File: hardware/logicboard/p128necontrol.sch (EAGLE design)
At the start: 57 parts, among them IC1 74LS158N, IC10 74LS595D, IC11 74LS595D, IC12 74LS595D, IC13 74LS595D, IC14 74LS595D, IC15 74LS595D, IC16 74LS595D, IC17 74LS595D, IC2 74LS595D, IC3 74LS595D, IC4 74LS595D, IC5 74LS595D, IC6 74LS595D, IC7 74LS595D, IC8 74LS595D, IC9 74LS595D, J2 DIN5

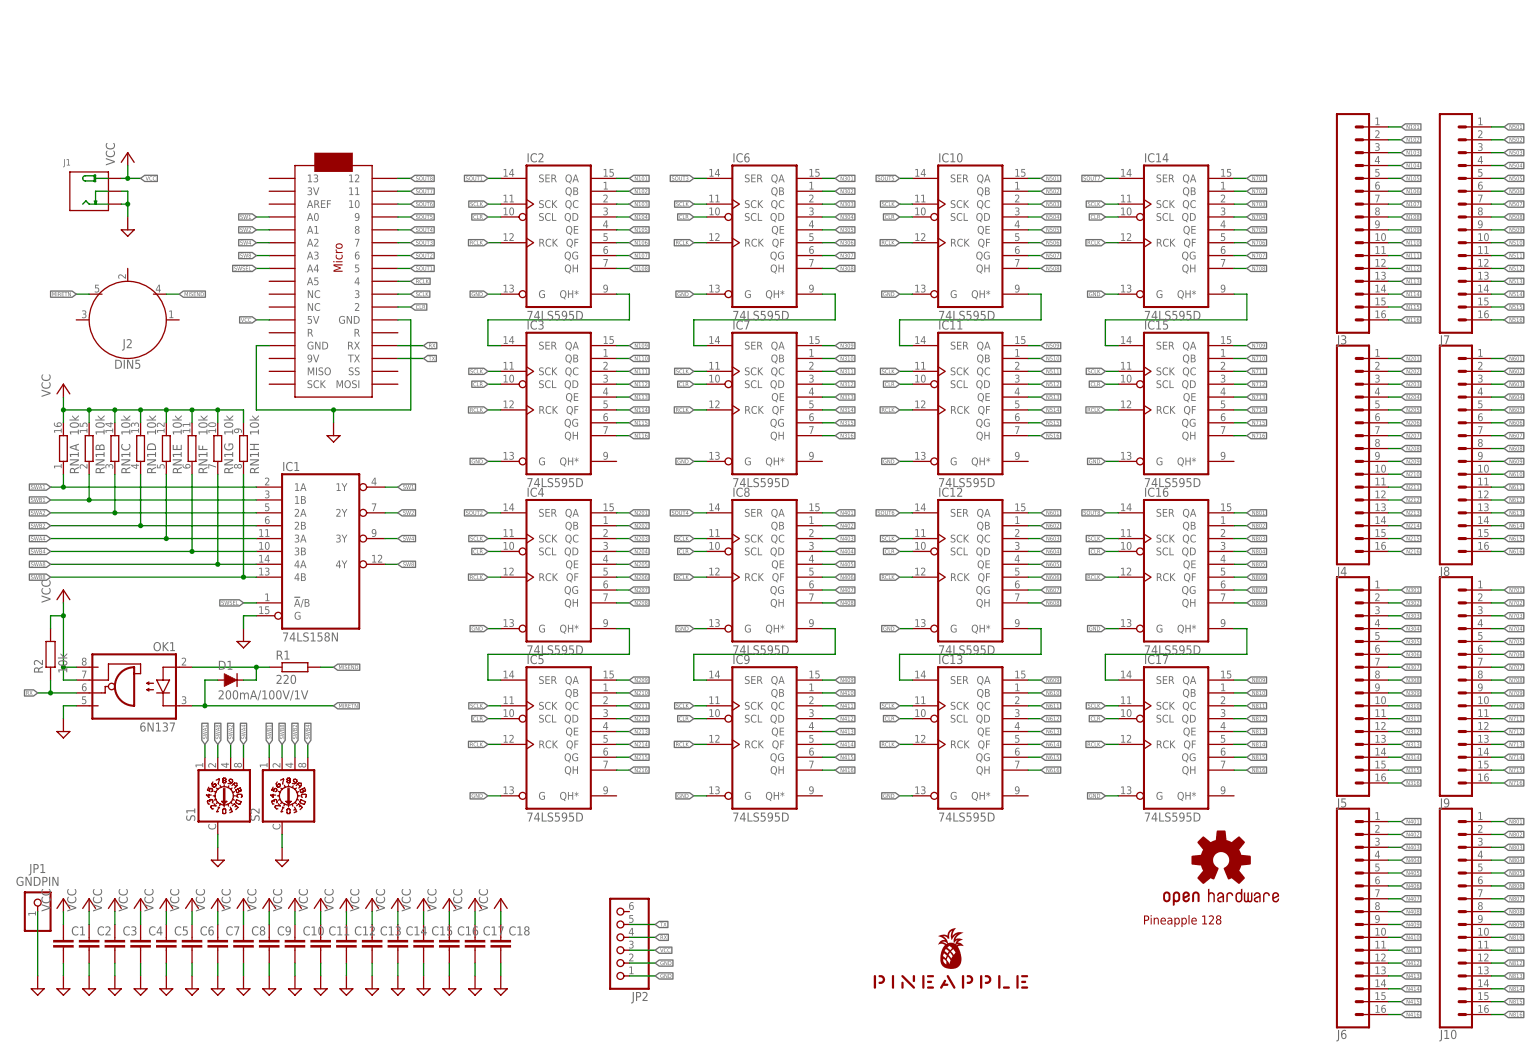
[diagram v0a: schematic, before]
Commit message: Nocontrol 128-ch out.
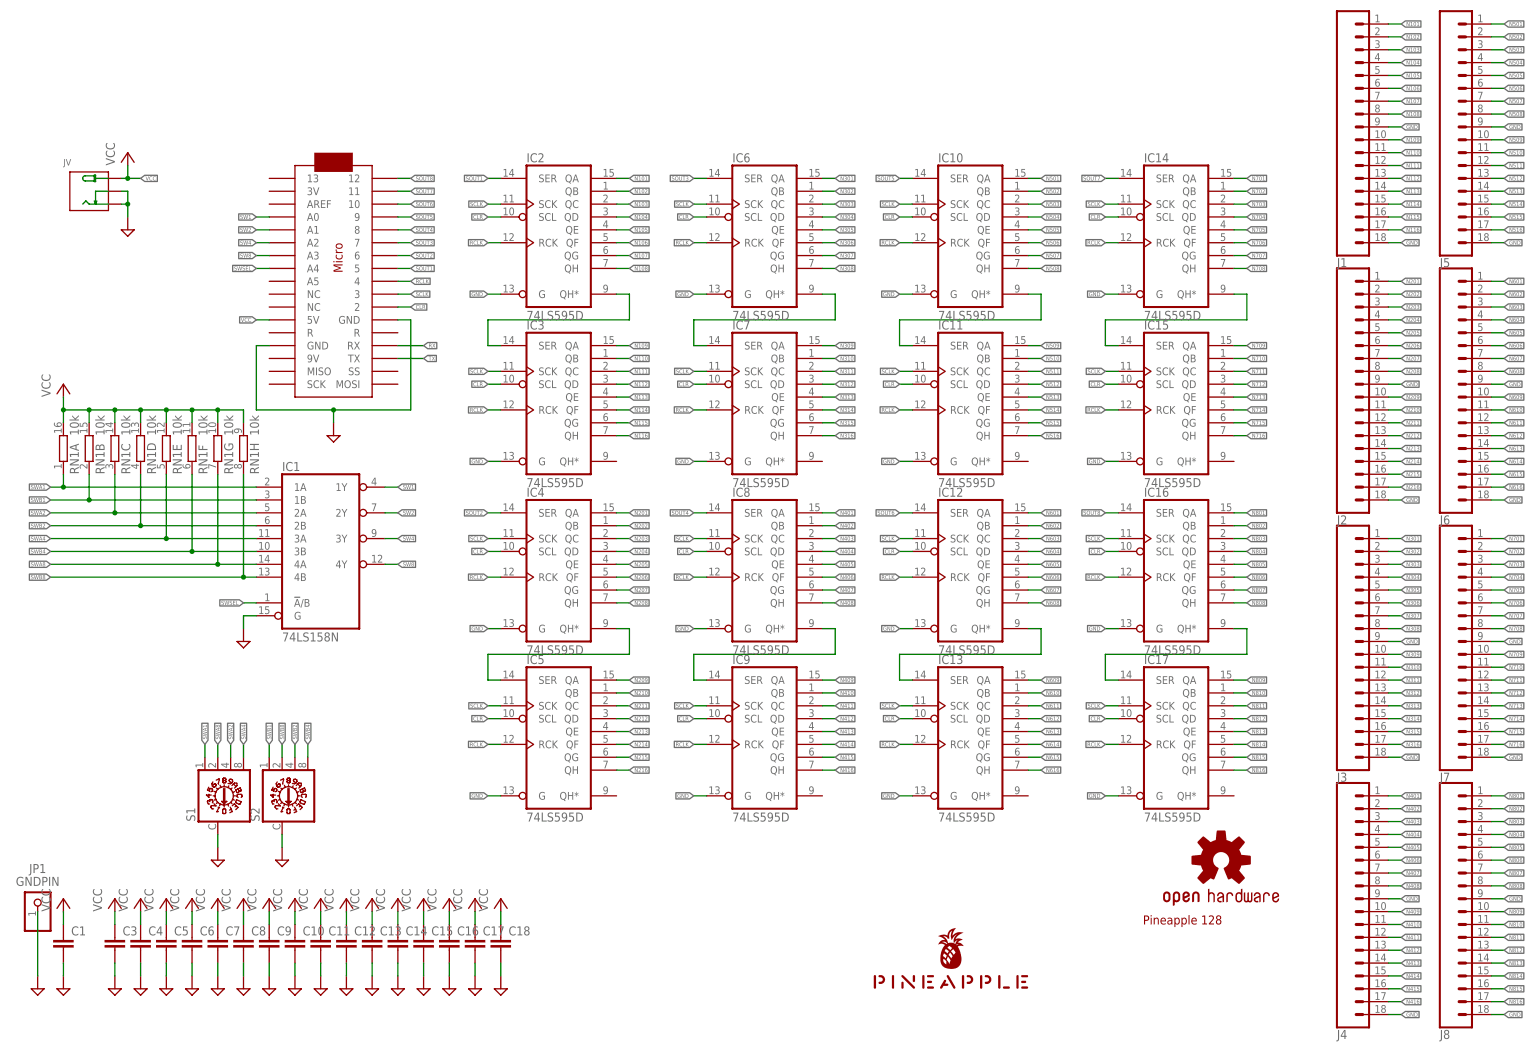
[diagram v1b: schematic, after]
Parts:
- removed C2: (no value), resistor:C-EU025-024X044
- removed D1: 200mA/100V/1V, SparkFun-DiscreteSemi:DIODE-1N4148
- removed J10, J9: (no value), SparkFun-Connectors:CONN_16
- removed JP2: (no value), pinhead:PINHD-1X6
- removed OK1: 6N137, optocoupler:6N137
- removed R1: 220, resistor:R-EU_0204/5
- removed R2: 10k, resistor:R-EU_0204/5
- added JV: (no value), Seeed-Connector:JACK-DC-005'DC-005'
- J1: device Seeed-Connector:JACK-DC-005'DC-005' -> SparkFun-Connectors:CONN_18
- J2: value DIN5 -> (none); device SparkFun-Connectors:DIN5 -> SparkFun-Connectors:CONN_18
- J3, J4, J5, J6, J7, J8: device SparkFun-Connectors:CONN_16 -> SparkFun-Connectors:CONN_18
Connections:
- removed net MIRETN: D1.A, J2.5, OK1.C
- removed net MISEND: J2.4, R1.2
- removed net N$1: D1.C, OK1.A, R1.1
- net GND: now also J1.18, J1.9, J2.18, J2.9, J3.18, J3.9, J4.18, J4.9, J5.18, J5.9, J6.18, J6.9, J7.18, J7.9, J8.18, J8.9, JV.-, JV.CDN; no longer C2.2, J1.-, J1.CDN, JP2.1, JP2.2, OK1.GND
- net N101: now also J1.1; no longer J3.1
- net N102: now also J1.2; no longer J3.2
- net N103: now also J1.3; no longer J3.3
- net N104: now also J1.4; no longer J3.4
- net N105: now also J1.5; no longer J3.5
- net N106: now also J1.6; no longer J3.6
- net N107: now also J1.7; no longer J3.7
- net N108: now also J1.8; no longer J3.8
- net N109: now also J1.10; no longer J3.9
- net N110: now also J1.11; no longer J3.10
- net N111: now also J1.12; no longer J3.11
- net N112: now also J1.13; no longer J3.12
- net N113: now also J1.14; no longer J3.13
- net N114: now also J1.15; no longer J3.14
- net N115: now also J1.16; no longer J3.15
- net N116: now also J1.17; no longer J3.16
- net N201: now also J2.1; no longer J4.1
- net N202: now also J2.2; no longer J4.2
- net N203: now also J2.3; no longer J4.3
- net N204: now also J2.4; no longer J4.4
- net N205: now also J2.5; no longer J4.5
- net N206: now also J2.6; no longer J4.6
- net N207: now also J2.7; no longer J4.7
- net N208: now also J2.8; no longer J4.8
- net N209: now also J2.10; no longer J4.9
- net N210: now also J2.11; no longer J4.10
- net N211: now also J2.12; no longer J4.11
- net N212: now also J2.13; no longer J4.12
- net N213: now also J2.14; no longer J4.13
- net N214: now also J2.15; no longer J4.14
- net N215: now also J2.16; no longer J4.15
- net N216: now also J2.17; no longer J4.16
- net N301: now also J3.1; no longer J5.1
- net N302: now also J3.2; no longer J5.2
- net N303: now also J3.3; no longer J5.3
- net N304: now also J3.4; no longer J5.4
- net N305: now also J3.5; no longer J5.5
- net N306: now also J3.6; no longer J5.6
- net N307: now also J3.7; no longer J5.7
- net N308: now also J3.8; no longer J5.8
- net N309: now also J3.10; no longer J5.9
- net N310: now also J3.11; no longer J5.10
- net N311: now also J3.12; no longer J5.11
- net N312: now also J3.13; no longer J5.12
- net N313: now also J3.14; no longer J5.13
- net N314: now also J3.15; no longer J5.14
- net N315: now also J3.16; no longer J5.15
- net N316: now also J3.17; no longer J5.16
- net N401: now also J4.1; no longer J6.1
- net N402: now also J4.2; no longer J6.2
- net N403: now also J4.3; no longer J6.3
- net N404: now also J4.4; no longer J6.4
- net N405: now also J4.5; no longer J6.5
- net N406: now also J4.6; no longer J6.6
- net N407: now also J4.7; no longer J6.7
- net N408: now also J4.8; no longer J6.8
- net N409: now also J4.10; no longer J6.9
- net N410: now also J4.11; no longer J6.10
- net N411: now also J4.12; no longer J6.11
- net N412: now also J4.13; no longer J6.12
- net N413: now also J4.14; no longer J6.13
- net N414: now also J4.15; no longer J6.14
- net N415: now also J4.16; no longer J6.15
- net N416: now also J4.17; no longer J6.16
- net N501: now also J5.1; no longer J7.1
- net N502: now also J5.2; no longer J7.2
- net N503: now also J5.3; no longer J7.3
- net N504: now also J5.4; no longer J7.4
- net N505: now also J5.5; no longer J7.5
- net N506: now also J5.6; no longer J7.6
- net N507: now also J5.7; no longer J7.7
- net N508: now also J5.8; no longer J7.8
- net N509: now also J5.10; no longer J7.9
- net N510: now also J5.11; no longer J7.10
- net N511: now also J5.12; no longer J7.11
- net N512: now also J5.13; no longer J7.12
- net N513: now also J5.14; no longer J7.13
- net N514: now also J5.15; no longer J7.14
- net N515: now also J5.16; no longer J7.15
- net N516: now also J5.17; no longer J7.16
- net N601: now also J6.1; no longer J8.1
- net N602: now also J6.2; no longer J8.2
- net N603: now also J6.3; no longer J8.3
- net N604: now also J6.4; no longer J8.4
- net N605: now also J6.5; no longer J8.5
- net N606: now also J6.6; no longer J8.6
- net N607: now also J6.7; no longer J8.7
- net N608: now also J6.8; no longer J8.8
- net N609: now also J6.10; no longer J8.9
- net N610: now also J6.11; no longer J8.10
- net N611: now also J6.12; no longer J8.11
- net N612: now also J6.13; no longer J8.12
- net N613: now also J6.14; no longer J8.13
- net N614: now also J6.15; no longer J8.14
- net N615: now also J6.16; no longer J8.15
- net N616: now also J6.17; no longer J8.16
- net N701: now also J7.1; no longer J9.1
- net N702: now also J7.2; no longer J9.2
- net N703: now also J7.3; no longer J9.3
- net N704: now also J7.4; no longer J9.4
- net N705: now also J7.5; no longer J9.5
- net N706: now also J7.6; no longer J9.6
- net N707: now also J7.7; no longer J9.7
- net N708: now also J7.8; no longer J9.8
- net N709: now also J7.10; no longer J9.9
- net N710: now also J7.11; no longer J9.10
- net N711: now also J7.12; no longer J9.11
- net N712: now also J7.13; no longer J9.12
- net N713: now also J7.14; no longer J9.13
- net N714: now also J7.15; no longer J9.14
- net N715: now also J7.16; no longer J9.15
- net N716: now also J7.17; no longer J9.16
- net N801: now also J8.1; no longer J10.1
- net N802: now also J8.2; no longer J10.2
- net N803: now also J8.3; no longer J10.3
- net N804: now also J8.4; no longer J10.4
- net N805: now also J8.5; no longer J10.5
- net N806: now also J8.6; no longer J10.6
- net N807: now also J8.7; no longer J10.7
- net N808: now also J8.8; no longer J10.8
- net N809: now also J8.10; no longer J10.9
- net N810: now also J8.11; no longer J10.10
- net N811: now also J8.12; no longer J10.11
- net N812: now also J8.13; no longer J10.12
- net N813: now also J8.14; no longer J10.13
- net N814: now also J8.15; no longer J10.14
- net N815: now also J8.16; no longer J10.15
- net N816: now also J8.17; no longer J10.16
- net RX: no longer JP2.4, OK1.VO, R2.1
- net TX: no longer JP2.5
- net VCC: now also JV.+; no longer C2.1, J1.+, JP2.3, OK1.VCC, OK1.VE, R2.2

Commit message: First working necontrol.
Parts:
- removed C10, C11, C12, C13, C14, C15, C16, C17, C18, C9: (no value), resistor:C-EUC2012
- removed IC10, IC11, IC12, IC13, IC14, IC15, IC16, IC17, IC9: 74LS595D, 74xx-us:74LS595D
- removed RN1: 10k, resistor-dil:8R-N
- removed S1, S2: (no value), switch-dil:A1353HEX
- added C2: (no value), resistor:C-EU025-024X044
- added SV1, SV2, SV3: (no value), con-ml:ML14E
- C3, C4, C5, C6, C7, C8: device resistor:C-EUC2012 -> resistor:C-EU025-024X044
- IC1: value 74LS158N -> 74LS595N; device 74xx-us:74LS158N -> 74xx-us:74LS595N
- IC2, IC3, IC4, IC5, IC6, IC7, IC8: value 74LS595D -> 74LS595N; device 74xx-us:74LS595D -> 74xx-us:74LS595N
- J1, J2, J3, J4, J5, J6, J7, J8: device SparkFun-Connectors:CONN_18 -> SparkFun-Connectors:CONN_10"
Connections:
- removed net N$2: IC2A.QH*, IC3A.SER
- removed net N$3: IC4A.QH*, IC5A.SER
- removed net N$4: IC6A.QH*, IC7A.SER
- removed net N$5: IC8A.QH*, IC9A.SER
- removed net N$6: IC10A.QH*, IC11A.SER
- removed net N$7: IC12A.QH*, IC13A.SER
- removed net N$8: IC14A.QH*, IC15A.SER
- removed net N$9: IC16A.QH*, IC17A.SER
- removed net N109: IC3A.QA, J1.10
- removed net N110: IC3A.QB, J1.11
- removed net N111: IC3A.QC, J1.12
- removed net N112: IC3A.QD, J1.13
- removed net N113: IC3A.QE, J1.14
- removed net N114: IC3A.QF, J1.15
- removed net N115: IC3A.QG, J1.16
- removed net N116: IC3A.QH, J1.17
- removed net N209: IC5A.QA, J2.10
- removed net N210: IC5A.QB, J2.11
- removed net N211: IC5A.QC, J2.12
- removed net N212: IC5A.QD, J2.13
- removed net N213: IC5A.QE, J2.14
- removed net N214: IC5A.QF, J2.15
- removed net N215: IC5A.QG, J2.16
- removed net N216: IC5A.QH, J2.17
- removed net N309: IC7A.QA, J3.10
- removed net N310: IC7A.QB, J3.11
- removed net N311: IC7A.QC, J3.12
- removed net N312: IC7A.QD, J3.13
- removed net N313: IC7A.QE, J3.14
- removed net N314: IC7A.QF, J3.15
- removed net N315: IC7A.QG, J3.16
- removed net N316: IC7A.QH, J3.17
- removed net N409: IC9A.QA, J4.10
- removed net N410: IC9A.QB, J4.11
- removed net N411: IC9A.QC, J4.12
- removed net N412: IC9A.QD, J4.13
- removed net N413: IC9A.QE, J4.14
- removed net N414: IC9A.QF, J4.15
- removed net N415: IC9A.QG, J4.16
- removed net N416: IC9A.QH, J4.17
- removed net N509: IC11A.QA, J5.10
- removed net N510: IC11A.QB, J5.11
- removed net N511: IC11A.QC, J5.12
- removed net N512: IC11A.QD, J5.13
- removed net N513: IC11A.QE, J5.14
- removed net N514: IC11A.QF, J5.15
- removed net N515: IC11A.QG, J5.16
- removed net N516: IC11A.QH, J5.17
- removed net N609: IC13A.QA, J6.10
- removed net N610: IC13A.QB, J6.11
- removed net N611: IC13A.QC, J6.12
- removed net N612: IC13A.QD, J6.13
- removed net N613: IC13A.QE, J6.14
- removed net N614: IC13A.QF, J6.15
- removed net N615: IC13A.QG, J6.16
- removed net N616: IC13A.QH, J6.17
- removed net N709: IC15A.QA, J7.10
- removed net N710: IC15A.QB, J7.11
- removed net N711: IC15A.QC, J7.12
- removed net N712: IC15A.QD, J7.13
- removed net N713: IC15A.QE, J7.14
- removed net N714: IC15A.QF, J7.15
- removed net N715: IC15A.QG, J7.16
- removed net N716: IC15A.QH, J7.17
- removed net N809: IC17A.QA, J8.10
- removed net N810: IC17A.QB, J8.11
- removed net N811: IC17A.QC, J8.12
- removed net N812: IC17A.QD, J8.13
- removed net N813: IC17A.QE, J8.14
- removed net N814: IC17A.QF, J8.15
- removed net N815: IC17A.QG, J8.16
- removed net N816: IC17A.QH, J8.17
- removed net SWA1: IC1A.1A, RN1A.1, S1.1
- removed net SWA2: IC1A.2A, RN1C.1, S1.4
- removed net SWA4: IC1A.3A, RN1E.1, S1.8
- removed net SWA8: IC1A.4A, RN1G.1, S1.2
- removed net SWB1: IC1A.1B, RN1B.1, S2.1
- removed net SWB2: IC1A.2B, RN1D.1, S2.4
- removed net SWB4: IC1A.3B, RN1F.1, S2.8
- removed net SWB8: IC1A.4B, RN1H.1, S2.2
- new net SIN1: IC1A.SER, SV2-6.S
- new net SIN2: IC2A.SER, SV2-7.S
- new net SIN3: IC3A.SER, SV2-8.S
- new net SIN4: IC4A.SER, SV2-9.S
- new net SIN5: IC5A.SER, SV2-10.S
- new net SIN6: IC6A.SER, SV2-11.S
- new net SIN7: IC7A.SER, SV2-12.S
- new net SIN8: IC8A.SER, SV2-13.S
- new net XOUT1: IC1A.QH*, SV3-6.S
- new net XOUT2: IC2A.QH*, SV3-7.S
- new net XOUT3: IC3A.QH*, SV3-8.S
- new net XOUT4: IC4A.QH*, SV3-9.S
- new net XOUT5: IC5A.QH*, SV3-10.S
- new net XOUT6: IC6A.QH*, SV3-11.S
- new net XOUT7: IC7A.QH*, SV3-12.S
- new net XOUT8: IC8A.QH*, SV3-13.S
- net CLR: now also IC1A.SCL, SV1-3.S, SV2-3.S, SV3-3.S; no longer IC10A.SCL, IC11A.SCL, IC12A.SCL, IC13A.SCL, IC14A.SCL, IC15A.SCL, IC16A.SCL, IC17A.SCL, IC9A.SCL
- net GND: now also C2.2, J1.10, J2.10, J3.10, J4.10, J5.10, J6.10, J7.10, J8.10, SV1-14.S, SV1-2.S, SV2-14.S, SV2-2.S, SV3-14.S, SV3-2.S; no longer C10.2, C11.2, C12.2, C13.2, C14.2, C15.2, C16.2, C17.2, C18.2, C9.2, IC10A.G, IC11A.G, IC12A.G, IC13A.G, IC14A.G, IC15A.G, IC16A.G, IC17A.G, IC9A.G, J1.18, J2.18, J3.18, J4.18, J5.18, J6.18, J7.18, J8.18, S1.C, S2.C
- net N101: now also IC1A.QA; no longer IC2A.QA
- net N102: now also IC1A.QB; no longer IC2A.QB
- net N103: now also IC1A.QC; no longer IC2A.QC
- net N104: now also IC1A.QD; no longer IC2A.QD
- net N105: now also IC1A.QE; no longer IC2A.QE
- net N106: now also IC1A.QF; no longer IC2A.QF
- net N107: now also IC1A.QG; no longer IC2A.QG
- net N108: now also IC1A.QH; no longer IC2A.QH
- net N201: now also IC2A.QA; no longer IC4A.QA
- net N202: now also IC2A.QB; no longer IC4A.QB
- net N203: now also IC2A.QC; no longer IC4A.QC
- net N204: now also IC2A.QD; no longer IC4A.QD
- net N205: now also IC2A.QE; no longer IC4A.QE
- net N206: now also IC2A.QF; no longer IC4A.QF
- net N207: now also IC2A.QG; no longer IC4A.QG
- net N208: now also IC2A.QH; no longer IC4A.QH
- net N301: now also IC3A.QA; no longer IC6A.QA
- net N302: now also IC3A.QB; no longer IC6A.QB
- net N303: now also IC3A.QC; no longer IC6A.QC
- net N304: now also IC3A.QD; no longer IC6A.QD
- net N305: now also IC3A.QE; no longer IC6A.QE
- net N306: now also IC3A.QF; no longer IC6A.QF
- net N307: now also IC3A.QG; no longer IC6A.QG
- net N308: now also IC3A.QH; no longer IC6A.QH
- net N401: now also IC4A.QA; no longer IC8A.QA
- net N402: now also IC4A.QB; no longer IC8A.QB
- net N403: now also IC4A.QC; no longer IC8A.QC
- net N404: now also IC4A.QD; no longer IC8A.QD
- net N405: now also IC4A.QE; no longer IC8A.QE
- net N406: now also IC4A.QF; no longer IC8A.QF
- net N407: now also IC4A.QG; no longer IC8A.QG
- net N408: now also IC4A.QH; no longer IC8A.QH
- net N501: now also IC5A.QA; no longer IC10A.QA
- net N502: now also IC5A.QB; no longer IC10A.QB
- net N503: now also IC5A.QC; no longer IC10A.QC
- net N504: now also IC5A.QD; no longer IC10A.QD
- net N505: now also IC5A.QE; no longer IC10A.QE
- net N506: now also IC5A.QF; no longer IC10A.QF
- net N507: now also IC5A.QG; no longer IC10A.QG
- net N508: now also IC5A.QH; no longer IC10A.QH
- net N601: now also IC6A.QA; no longer IC12A.QA
- net N602: now also IC6A.QB; no longer IC12A.QB
- net N603: now also IC6A.QC; no longer IC12A.QC
- net N604: now also IC6A.QD; no longer IC12A.QD
- net N605: now also IC6A.QE; no longer IC12A.QE
- net N606: now also IC6A.QF; no longer IC12A.QF
- net N607: now also IC6A.QG; no longer IC12A.QG
- net N608: now also IC6A.QH; no longer IC12A.QH
- net N701: now also IC7A.QA; no longer IC14A.QA
- net N702: now also IC7A.QB; no longer IC14A.QB
- net N703: now also IC7A.QC; no longer IC14A.QC
- net N704: now also IC7A.QD; no longer IC14A.QD
- net N705: now also IC7A.QE; no longer IC14A.QE
- net N706: now also IC7A.QF; no longer IC14A.QF
- net N707: now also IC7A.QG; no longer IC14A.QG
- net N708: now also IC7A.QH; no longer IC14A.QH
- net N801: now also IC8A.QA; no longer IC16A.QA
- net N802: now also IC8A.QB; no longer IC16A.QB
- net N803: now also IC8A.QC; no longer IC16A.QC
- net N804: now also IC8A.QD; no longer IC16A.QD
- net N805: now also IC8A.QE; no longer IC16A.QE
- net N806: now also IC8A.QF; no longer IC16A.QF
- net N807: now also IC8A.QG; no longer IC16A.QG
- net N808: now also IC8A.QH; no longer IC16A.QH
- net RCLK: now also IC1A.RCK, SV1-5.S, SV2-5.S, SV3-5.S; no longer IC10A.RCK, IC11A.RCK, IC12A.RCK, IC13A.RCK, IC14A.RCK, IC15A.RCK, IC16A.RCK, IC17A.RCK, IC9A.RCK
- net SCLK: now also IC1A.SCK, SV1-4.S, SV2-4.S, SV3-4.S; no longer IC10A.SCK, IC11A.SCK, IC12A.SCK, IC13A.SCK, IC14A.SCK, IC15A.SCK, IC16A.SCK, IC17A.SCK, IC9A.SCK
- net SOUT1: now also SV1-6.S; no longer IC2A.SER
- net SOUT2: now also SV1-7.S; no longer IC4A.SER
- net SOUT3: now also SV1-8.S; no longer IC6A.SER
- net SOUT4: now also SV1-9.S; no longer IC8A.SER
- net SOUT5: now also SV1-10.S; no longer IC10A.SER
- net SOUT6: now also SV1-11.S; no longer IC12A.SER
- net SOUT7: now also SV1-12.S; no longer IC14A.SER
- net SOUT8: now also SV1-13.S; no longer IC16A.SER
- net SW1: no longer IC1A.1Y
- net SW2: no longer IC1A.2Y
- net SW4: no longer IC1A.3Y
- net SW8: no longer IC1A.4Y
- net SWSEL: no longer IC1A.!A!/B
- net VCC: now also C2.1, SV1-1.S, SV2-1.S, SV3-1.S; no longer C10.1, C11.1, C12.1, C13.1, C14.1, C15.1, C16.1, C17.1, C18.1, C9.1, RN1A.2, RN1B.2, RN1C.2, RN1D.2, RN1E.2, RN1F.2, RN1G.2, RN1H.2
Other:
- moved on the sheet: IC2, IC3, IC4, IC5, IC6, IC7, IC8
